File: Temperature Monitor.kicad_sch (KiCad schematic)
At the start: 7 parts, among them J1 Battery, J2 BME 280, J3 Display, SW1 Up, SW2 Down, SW3 Select, U2 XIAO-ESP32-C6-SMD

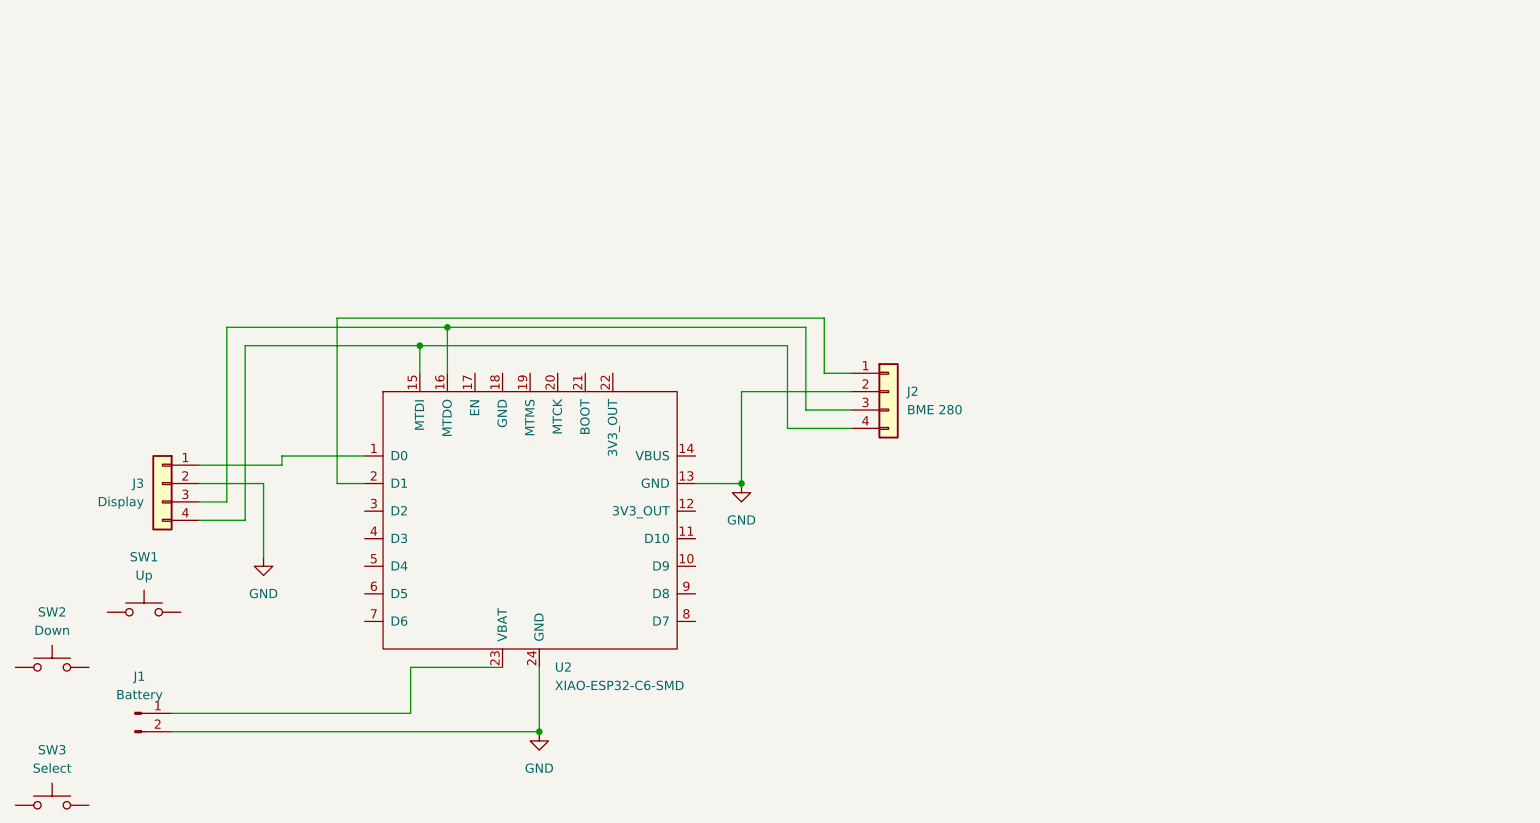
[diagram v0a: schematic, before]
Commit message: Added buttons
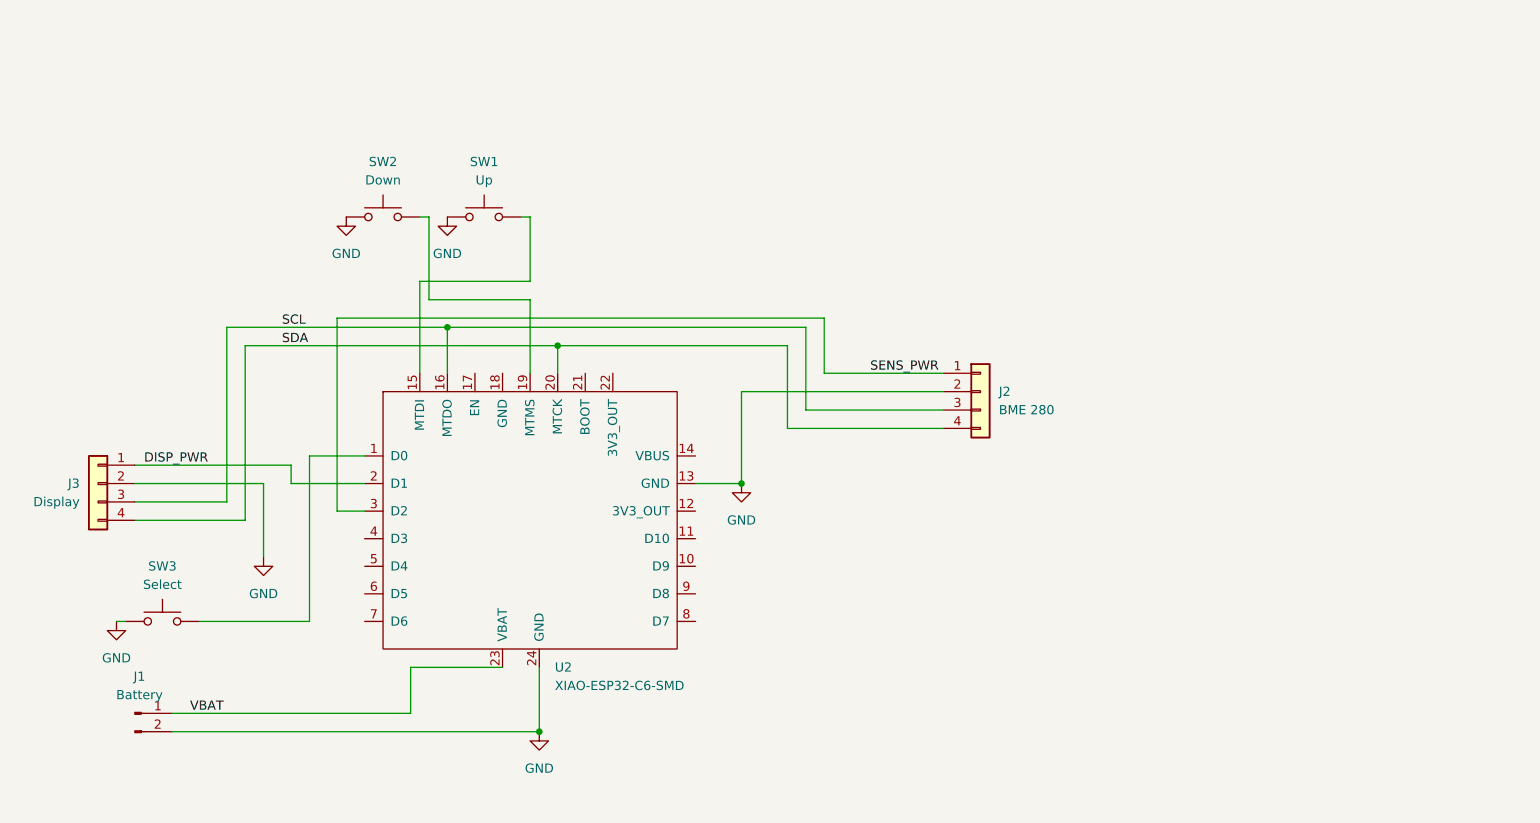
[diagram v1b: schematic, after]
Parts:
- SW1: footprint Button_Switch_SMD:SW_Push_1P1T_NO_CK_KSC6xxG -> Button_Switch_THT:SW_TH_Tactile_Omron_B3F-100x
- SW2: footprint Button_Switch_SMD:SW_Push_1P1T_NO_CK_KSC6xxG -> Button_Switch_THT:SW_TH_Tactile_Omron_B3F-102x
- SW3: footprint Button_Switch_SMD:SW_Push_1P1T_NO_CK_KSC6xxG -> Button_Switch_THT:SW_TH_Tactile_Omron_B3F-106x
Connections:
- net GND: now also SW1.1, SW2.1, SW3.1
- net at U2.1 (D0): now also SW3.2; no longer J3.1 (Pin_1)
- net SCL: now reaches J2.3 (Pin_3), J3.3 (Pin_3), U2.16 (MTDO)
- net SDA: now reaches J2.4 (Pin_4), J3.4 (Pin_4)
- net SDA: now also U2.20 (MTCK); no longer U2.15 (MTDI)
- net at SW2.2: now also U2.19 (MTMS)
- net DISP_PWR: now reaches U2.2 (D1)
- net DISP_PWR: now also J3.1 (Pin_1); no longer J2.1 (Pin_1)
- net VBAT: now reaches J1.1 (Pin_1), U2.23 (VBAT)
- net SENS_PWR: now reaches U2.3 (D2)
- net SENS_PWR: now also J2.1 (Pin_1)
- net at SW1.2: now also U2.15 (MTDI)
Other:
- moved on the sheet: J2, J3, SW1, SW2, SW3

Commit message: Added SCL resistor
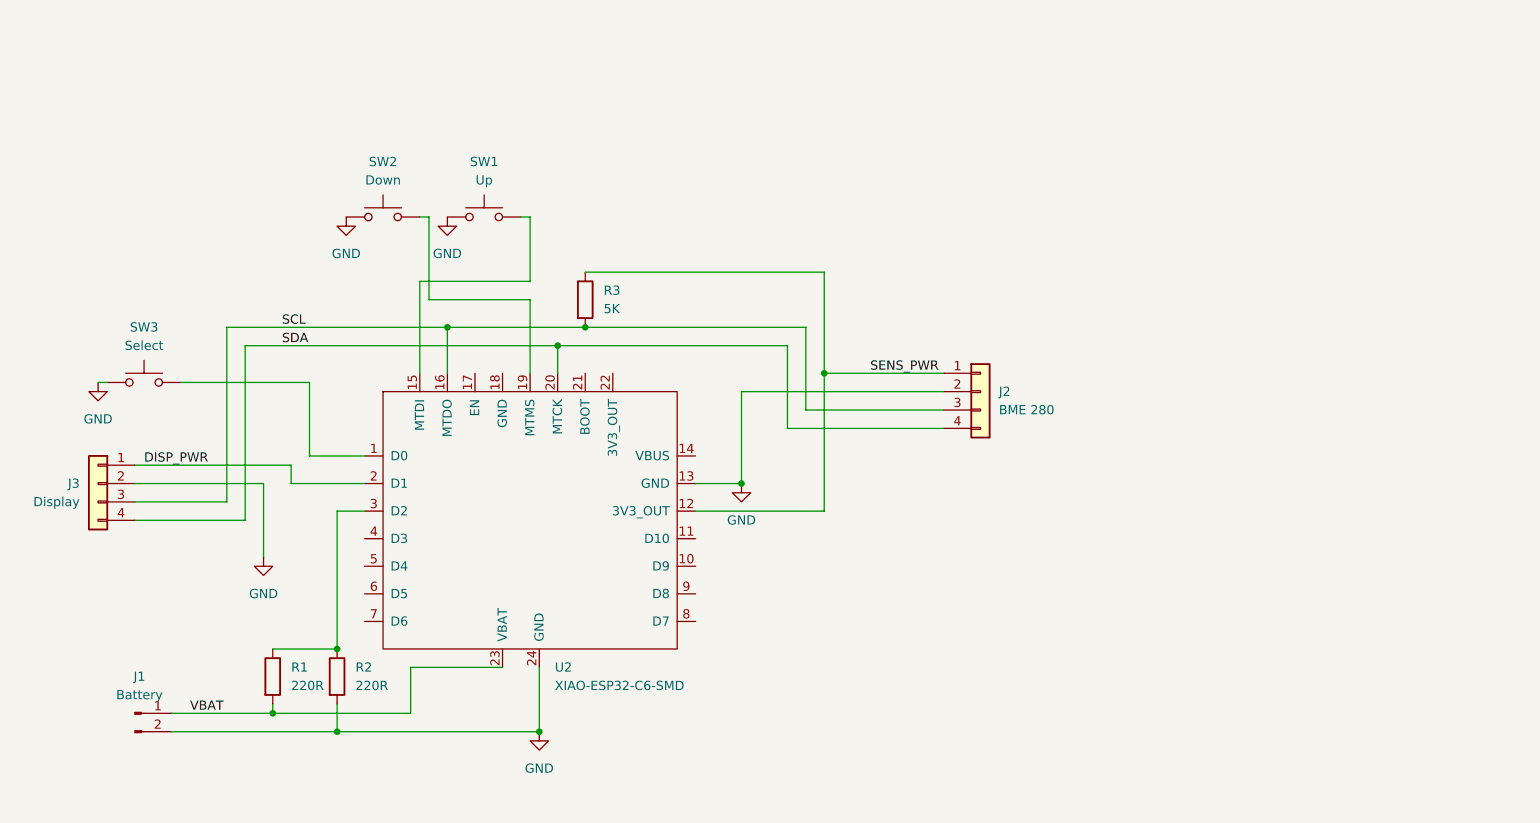
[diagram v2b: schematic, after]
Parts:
- added R1, R2: 220R, Resistor_THT:R_Axial_DIN0207_L6.3mm_D2.5mm_P7.62mm_Horizontal, symbol Device:R
- added R3: 5K, Resistor_THT:R_Axial_DIN0207_L6.3mm_D2.5mm_P7.62mm_Horizontal, symbol Device:R
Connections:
- net GND: now also R2.2
- net SCL: now also R3.2
- net SENS_PWR: now also U2.12 (3V3_OUT), R3.1; no longer U2.3 (D2)
- net VBAT: now also R1.2
- new net: R1.1, R2.1, U2.3 (D2)
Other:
- moved on the sheet: SW3

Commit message: Added Underside Traces
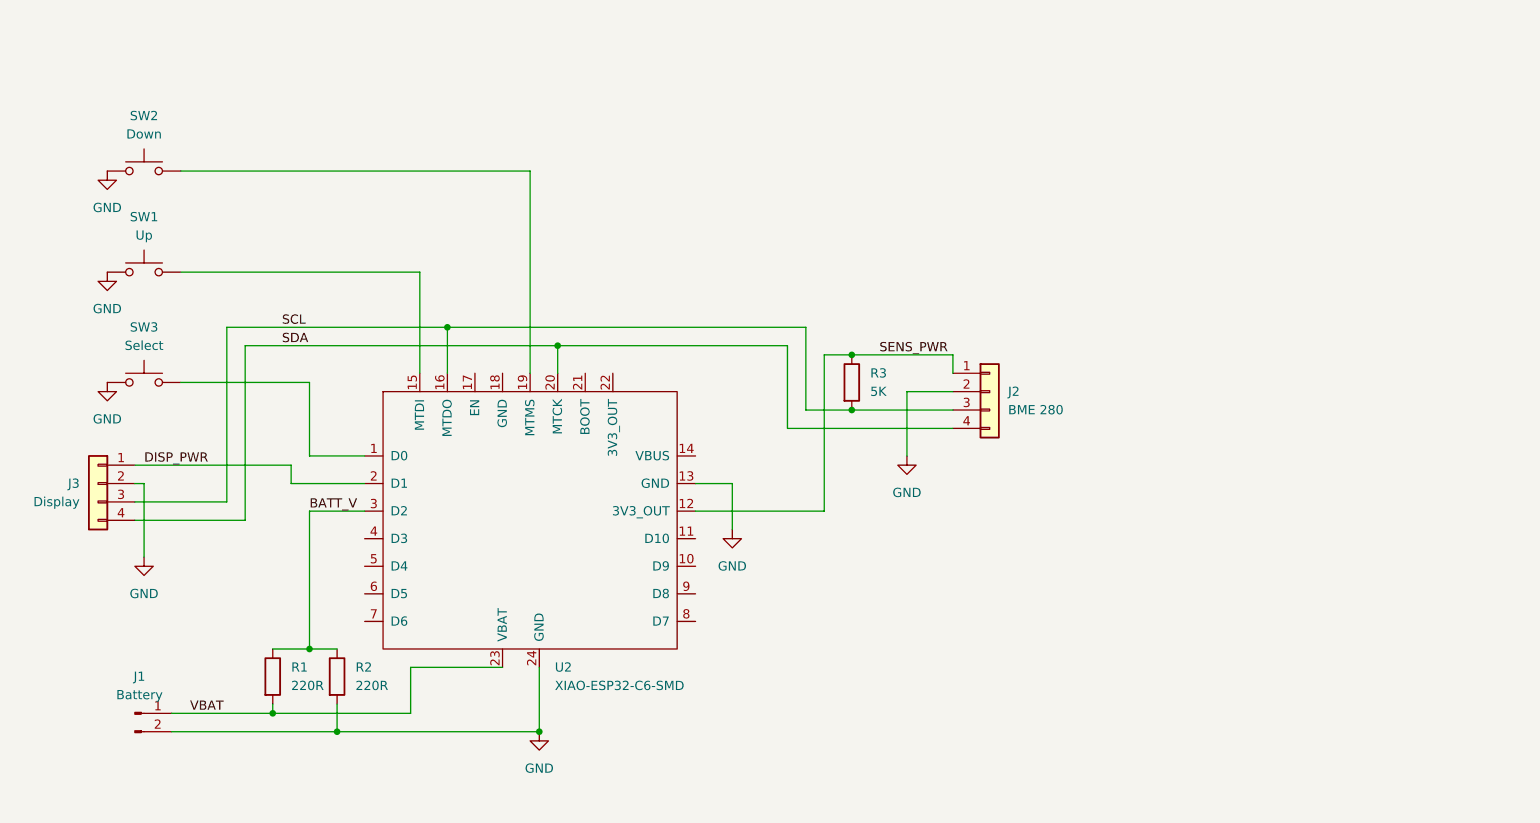
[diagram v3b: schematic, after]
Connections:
- net BATT_V: now reaches R1.1, R2.1, U2.3 (D2)
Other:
- moved on the sheet: J2, R3, SW1, SW2

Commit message: Updated to match SMB circuit
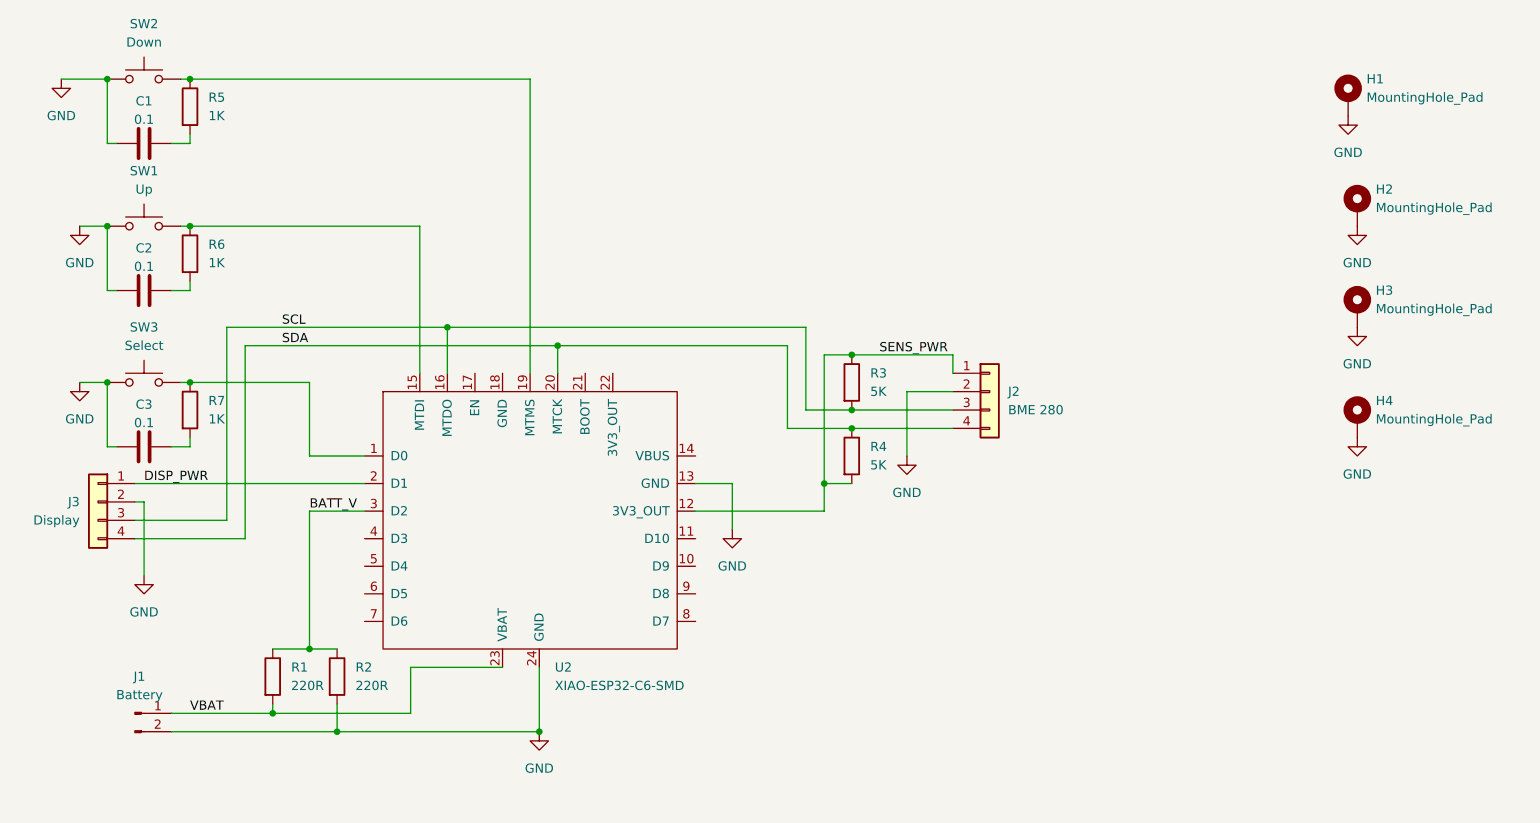
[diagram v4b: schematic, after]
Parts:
- added C1, C2, C3: 0.1, Capacitor_THT:CP_Radial_D5.0mm_P2.50mm, symbol Device:C
- added H1, H2, H3, H4: MountingHole_Pad, MountingHole:MountingHole_3.2mm_M3_ISO7380_Pad_TopBottom, symbol Mechanical:MountingHole_Pad
- added R4: 5K, Resistor_THT:R_Axial_DIN0207_L6.3mm_D2.5mm_P7.62mm_Horizontal, symbol Device:R
- added R5, R6, R7: 1K, Resistor_THT:R_Axial_DIN0207_L6.3mm_D2.5mm_P7.62mm_Horizontal, symbol Device:R
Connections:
- net GND: now also C1.1, C2.1, C3.1, H1.1, H2.1, H3.1, H4.1
- net SDA: now also R4.1
- net SENS_PWR: now also R4.2
- net at SW2.2, U2.19 (MTMS): now also R5.1
- net at SW3.2, U2.1 (D0): now also R7.1
- net at SW1.2, U2.15 (MTDI): now also R6.1
- new net: C2.2, R6.2
- new net: C3.2, R7.2
- new net: C1.2, R5.2
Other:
- moved on the sheet: J3, SW1, SW2

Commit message: General Improvements
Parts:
- C1, C2: value 0.1 -> 0.1U
- R1, R2: value 220R -> 220K
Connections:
- net Down: now reaches R5.1, SW2.2, U2.19 (MTMS)
- net Up: now reaches R6.1, SW1.2, U2.15 (MTDI)
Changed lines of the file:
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@@
+		)
+	)
+	(label "Down"
+		(at 87.63 22.86 0)
+		(effects
+			(font
+				(size 1.27 1.27)
+			)
+			(justify left bottom)
 		)
 	)
@@
 		)
 	)
+	(label "Up"
+		(at 88.9 43.18 0)
+		(effects
+			(font
+				(size 1.27 1.27)
+			)
+			(justify left bottom)
+		)
+	)
+	(label "Select"
+		(at 78.74 64.77 0)
+		(effects
+			(font
+				(size 1.27 1.27)
+			)
+			(justify left bottom)
+		)
+	)
 	(label "DISP_PWR"
 		(at 74.93 78.74 0)
@@
 			)
 		)
-		(property "Value" "0.1"
+		(property "Value" "0.1U"
 			(at 74.93 48.768 90)
 			(show_name no)
@@
 			)
 		)
-		(property "Value" "220R"
+		(property "Value" "220K"
 			(at 95.25 106.6799 0)
 			(show_name no)
@@
 			)
 		)
-		(property "Value" "0.1"
+		(property "Value" "0.1U"
 			(at 74.93 28.448 90)
 			(show_name no)
@@
 			)
 		)
-		(property "Value" "220R"
+		(property "Value" "220K"
 			(at 104.14 106.6799 0)
 			(show_name no)

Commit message: Trying to get changes to be comitted
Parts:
- C1, C2: value 0.1U -> 0.1uF
- C3: value 0.1 -> 0.1uF
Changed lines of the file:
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@@
 			)
 		)
-		(property "Value" "0.1U"
+		(property "Value" "0.1uF"
 			(at 74.93 48.768 90)
 			(show_name no)
@@
 			)
 		)
-		(property "Value" "0.1U"
+		(property "Value" "0.1uF"
 			(at 74.93 28.448 90)
 			(show_name no)
@@
 			)
 		)
-		(property "Value" "0.1"
+		(property "Value" "0.1uF"
 			(at 74.93 70.358 90)
 			(show_name no)
